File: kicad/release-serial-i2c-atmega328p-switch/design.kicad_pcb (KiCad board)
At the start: 2 copper layers, 38.9 x 16.4 mm, 34 parts, among them J17 Sense0, J3 RS232, J4 OUT0a, Q1 MMBT3904, Q2 FQP47P06, SW1 12V, U1 MCP1792T-33, U2 MCP1792T-5, U3 ATmega328P-AU, Y1 AB308-8.000MHZ

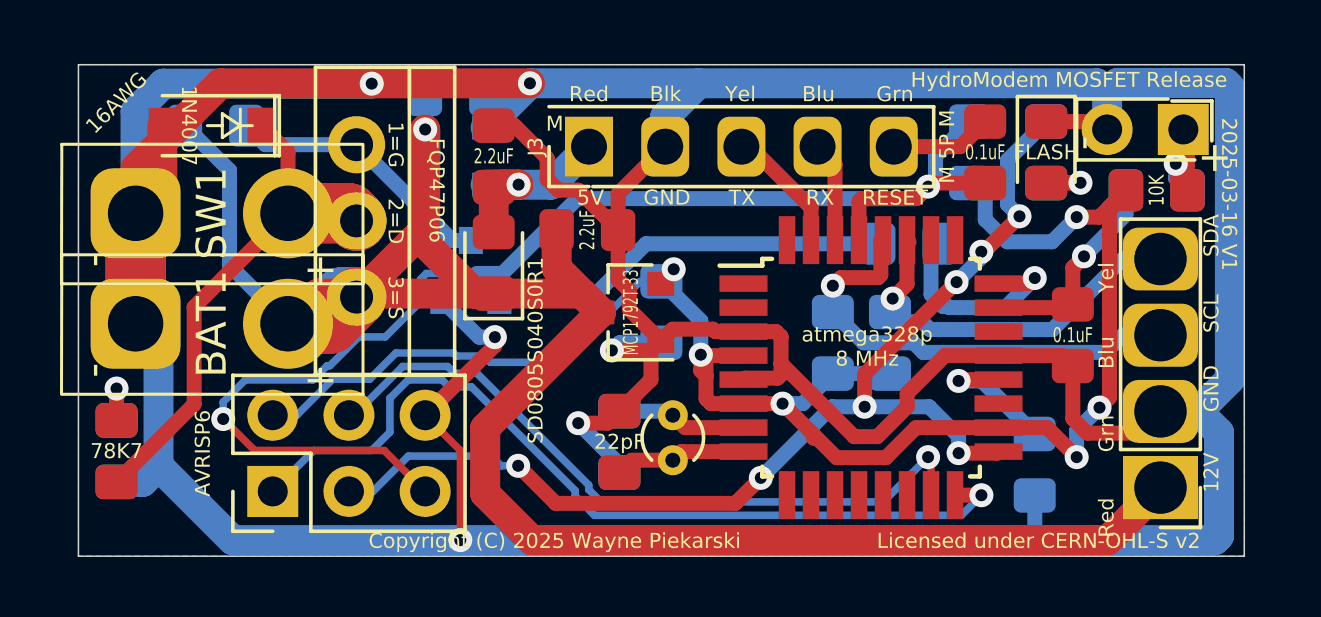
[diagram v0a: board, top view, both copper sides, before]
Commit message: Adjust AWG16 holes to 2.1mm as measured with tinned wires, AWG18 barely fit into these
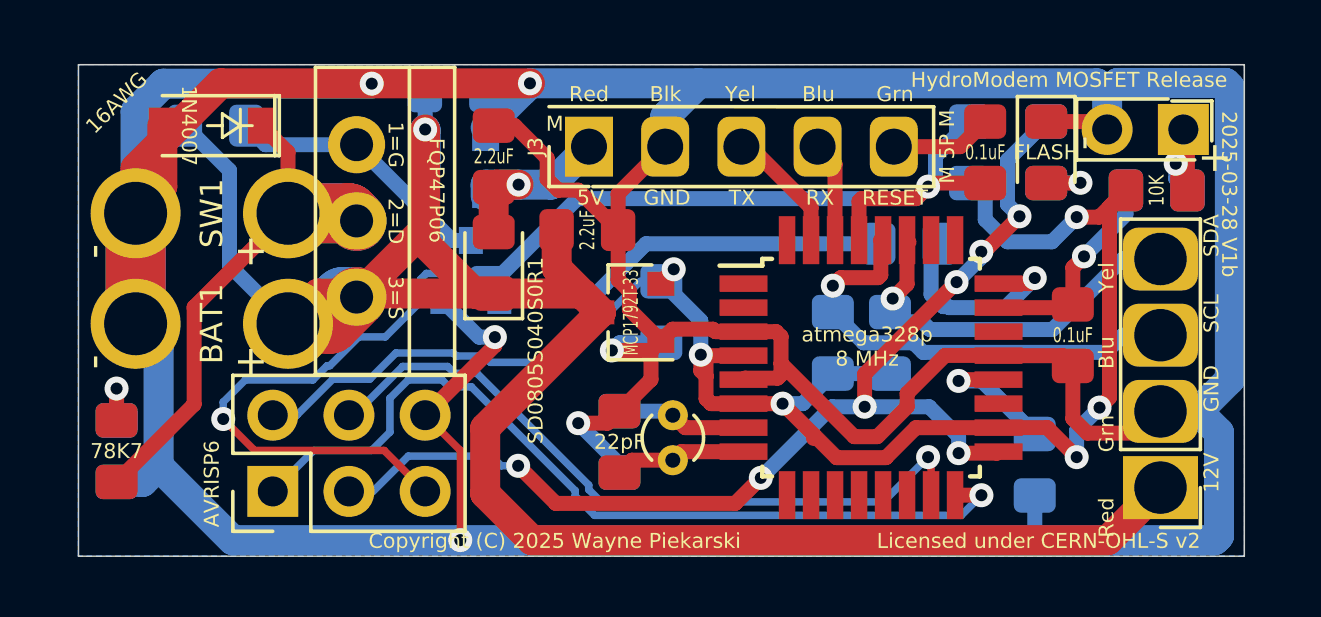
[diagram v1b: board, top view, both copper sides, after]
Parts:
- moved U2 0.38 mm to (113.3, 59.8)
- moved C3 0.13 mm to (113.3, 57.3)
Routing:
- net GND: track 191.2 -> 192.6 mm
- net 12V-In: track 71.4 -> 72.6 mm
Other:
- board text added: "2025-03-28 V1b"
- board text removed: "2025-03-16 V1"
